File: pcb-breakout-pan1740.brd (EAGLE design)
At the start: 30.5 x 22.1 mm, 3 parts, among them IC1 PAN1740

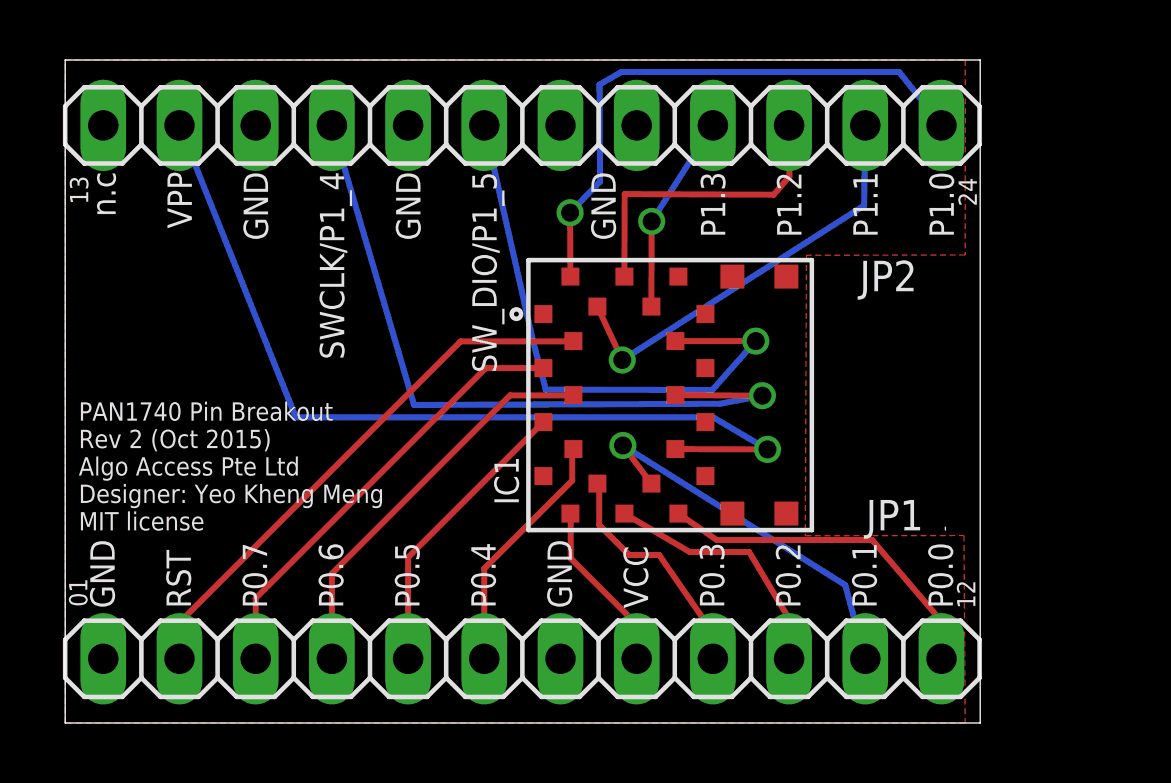
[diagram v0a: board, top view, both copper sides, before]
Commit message: position of pan1740
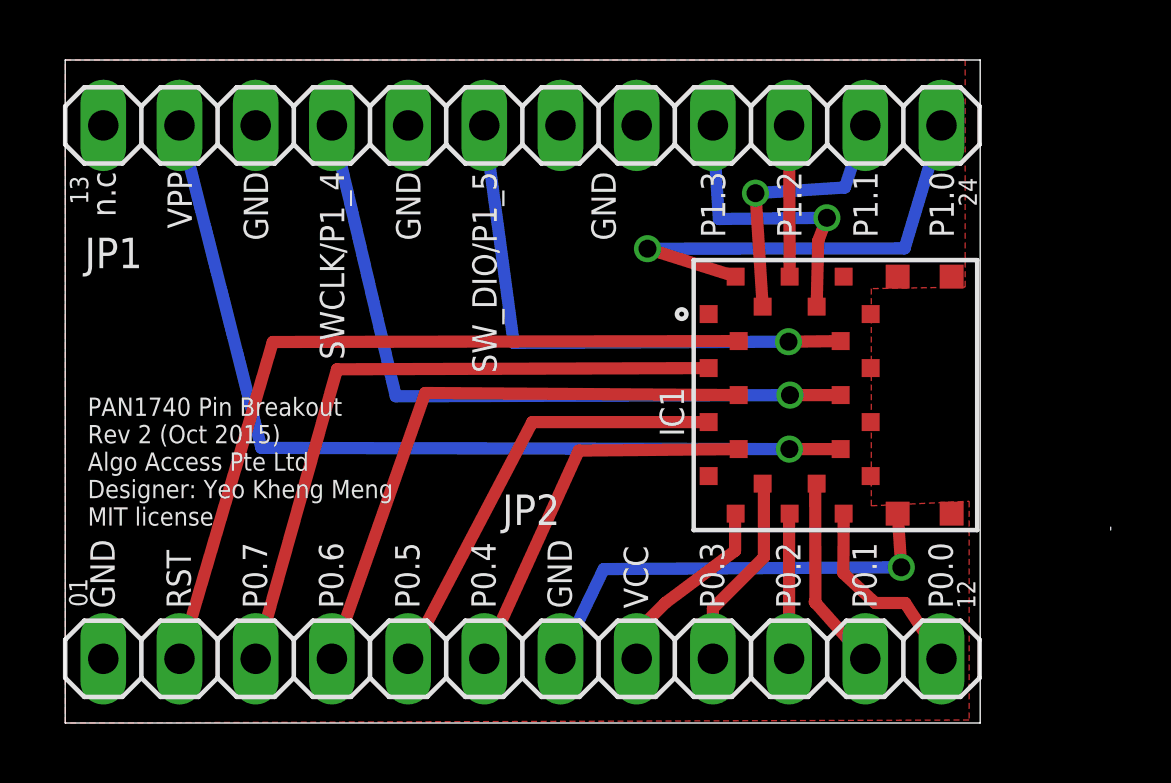
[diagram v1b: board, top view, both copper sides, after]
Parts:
- moved IC1 5.51 mm to (25.6, 10.9)
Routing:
- net GND: track 0.00 -> 15.0 mm, vias 0 -> 1
- net N$2: track 18.2 -> 26.5 mm
- net N$3: track 14.8 -> 22.4 mm
- net N$4: track 13.4 -> 19.8 mm
- net N$10: track 12.9 -> 6.54 mm, vias 1 -> 0
- net N$17: track 14.2 -> 8.95 mm
- net N$16: track 10.2 -> 5.04 mm
- net N$5: track 9.76 -> 14.8 mm
- net N$11: track 11.5 -> 6.66 mm
- net N$6: track 8.22 -> 13.0 mm
- net N$9: track 8.43 -> 4.85 mm
- net N$18: track 19.2 -> 15.9 mm
- net N$15: track 6.63 -> 9.74 mm
- net N$8: track 7.84 -> 6.56 mm
- net N$14: track 19.5 -> 18.2 mm
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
